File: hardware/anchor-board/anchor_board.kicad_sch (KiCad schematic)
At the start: 6 parts, among them U1 DWM3001C

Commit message: hw(anchor-board): capture §4.5 TLV75530 LDO; record MCU decision
- §4.5: U6 TLV75530 + C12/C13 1uF, C14 10uF, FB1 ferrite. The LDO OUT
  now drives the 3V0 rail, so the §4.1 3V0 PWR_FLAG placeholder is gone.
- New TLV75530 symbol (DQN / X2SON-4 pinout per the TLV755P datasheet).
- docs/mcu-tradeoff.md: decision to stay on the DWM3001C (not switch to
  DWM3000 + ESP32-C6), and solve developer onboarding by distributing
  pre-bootloadered boards. Includes the ESP32-C6 power model
  (~130-210 days vs ~290) and the antenna-delay self-cal finding.
- docs/datasheets/: 6 power-path datasheets committed (BQ24074, TPD4S014,
  TLV755P, DW01A, FS8205A, USB4105-GF-A).
- .kicad_pro filled out by KiCad on first open; .gitignore now excludes
  KiCad lock files and the VS Code .history/ dir.

ERC: 31 violations - 29 are U1's not-yet-captured §4.2-4.9 castellation
pins (expected WIP), 2 are footprint-not-found for the custom
DWM3001C / TLV75530 footprints (a layout-time task).
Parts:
- added C12, C13: 1uF, Capacitor_SMD:C_0603_1608Metric, symbol Device:C
- added C14: 10uF, Capacitor_SMD:C_0805_2012Metric, symbol Device:C
- added FB1: Ferrite Bead, Inductor_SMD:L_0603_1608Metric, symbol Device:L
- added U6: TLV75530, infinity-stumps:TLV75530_DQN, symbol infinity-stumps:TLV75530
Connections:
- net 3V0: now also C13.1, C14.1, U6.1 (OUT)
- net GND: now also C12.2, C13.2, C14.2, U6.2 (GND), U6.5 (PAD)
- new net VSYS: FB1.1
- new net VSYS_LDO: C12.1, FB1.2, U6.3 (EN), U6.4 (IN)

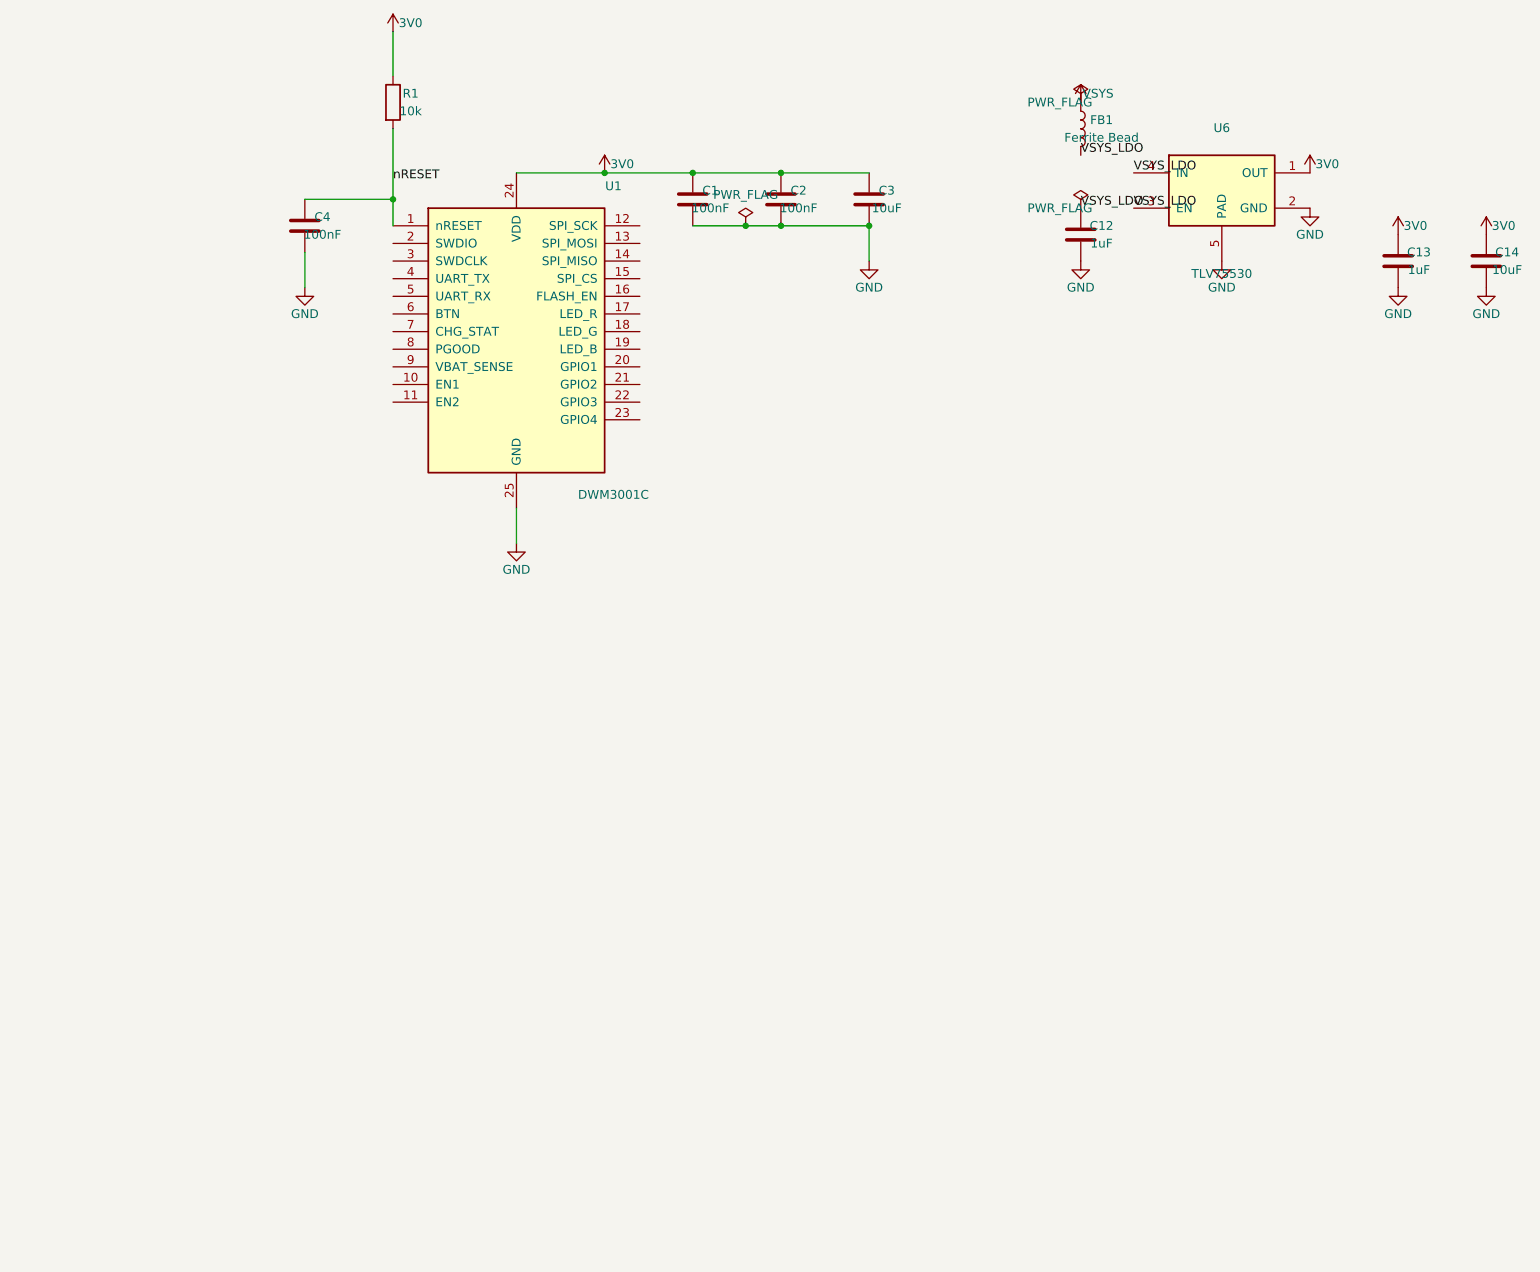
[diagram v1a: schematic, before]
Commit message: hw(anchor-board): capture §4.4 cell protection; add IC symbols; A3 sheet
- §4.4: BT1 18650 + U4 DW01A + U5 FS8205A + R13/C11/R14. DW01A+8205A
  back-to-back FET protection: cell+ -> VBAT, cell- -> BMINUS, the FET
  pair sits between BMINUS and system GND, DW_VCC fed via R13, current
  sense via R14, OD/OC gate drives, TD test pin no-connected.
- 5 new project symbols authored from docs/datasheets/: BQ24074, DW01A,
  FS8205A, USB4105-GF-A, TPD2E2U06. DW01A CS is a passive sense pin.
- Schematic sheet upgraded A4 -> A3 for the remaining functional blocks.

ERC: 32 violations - 29 are U1's not-yet-captured §4.2/4.3/4.6-4.8
castellation pins, 3 are footprint-not-found warnings for the custom
DWM3001C / TLV75530 / Keystone_1042 footprints (layout-time).
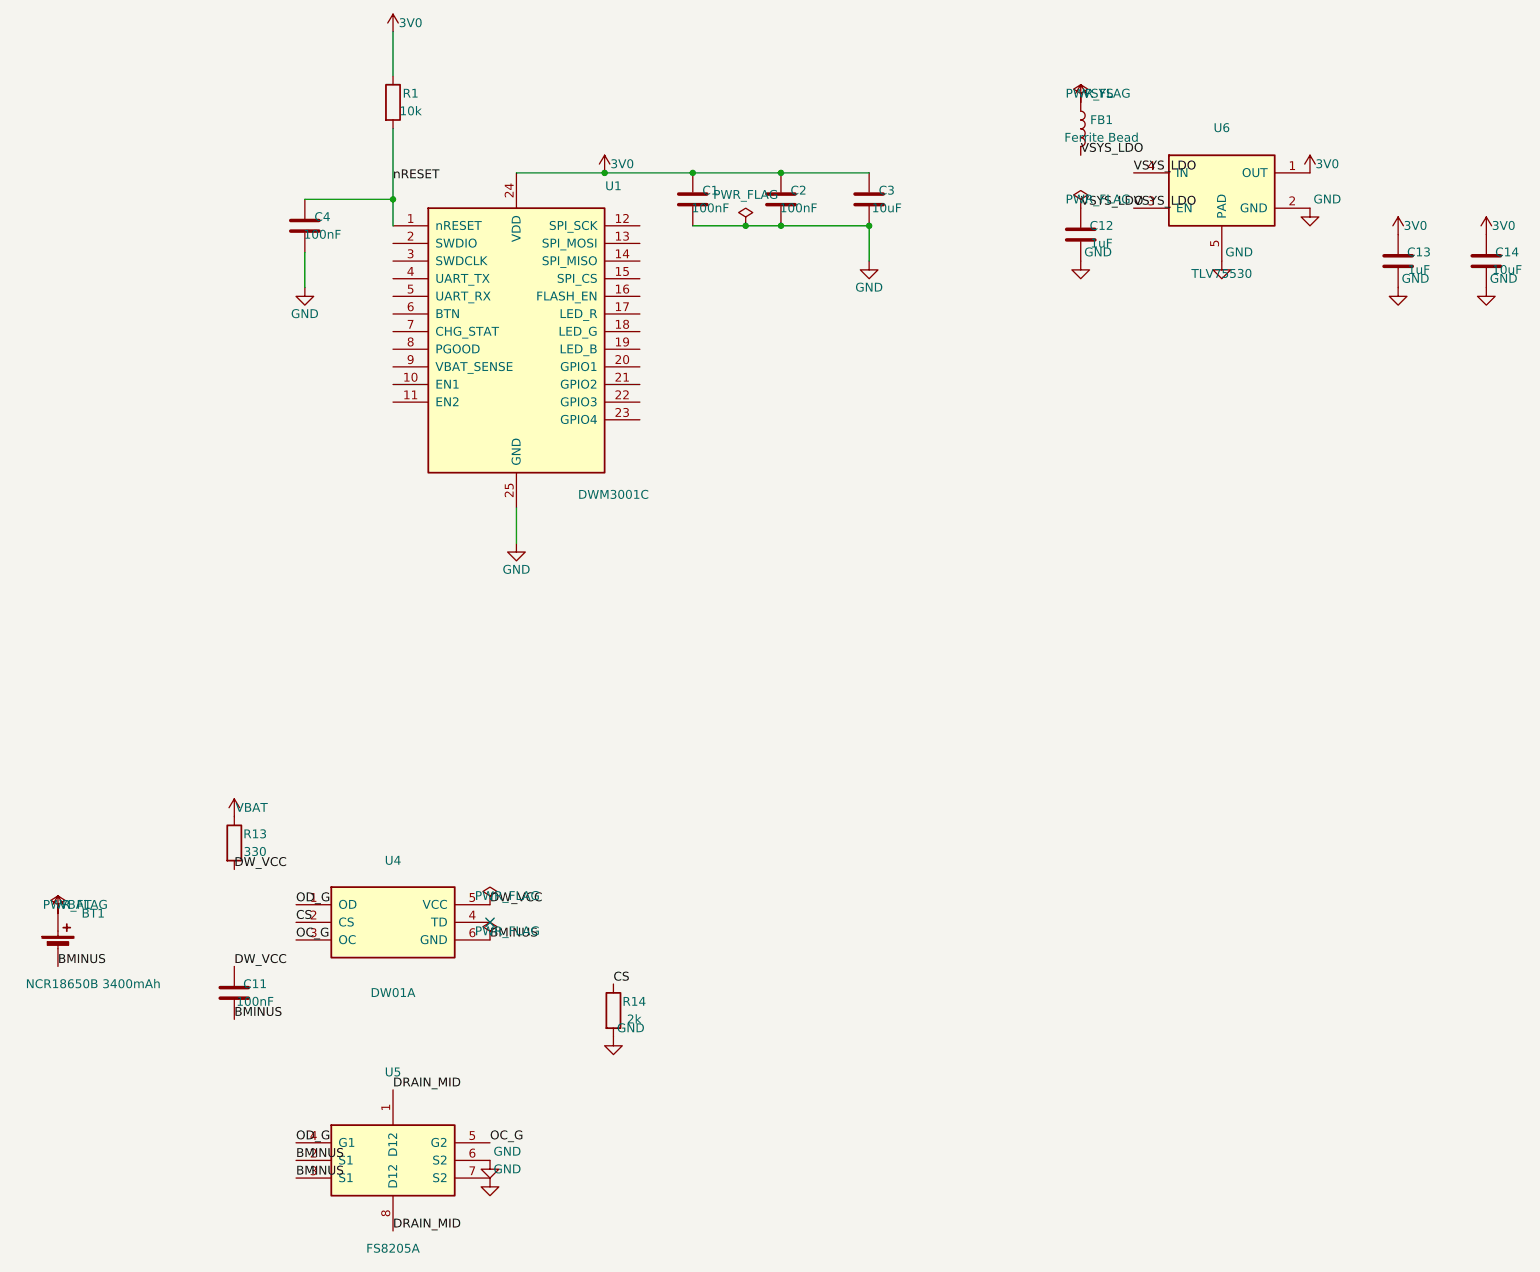
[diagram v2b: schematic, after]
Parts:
- added BT1: NCR18650B 3400mAh, infinity-stumps:Keystone_1042, symbol Device:Battery_Cell
- added C11: 100nF, Capacitor_SMD:C_0402_1005Metric, symbol Device:C
- added R13: 330, Resistor_SMD:R_0402_1005Metric, symbol Device:R
- added R14: 2k, Resistor_SMD:R_0402_1005Metric, symbol Device:R
- added U4: DW01A, Package_TO_SOT_SMD:SOT-23-6, symbol infinity-stumps:DW01A
- added U5: FS8205A, Package_SO:TSSOP-8_4.4x3mm_P0.65mm, symbol infinity-stumps:FS8205A
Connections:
- net GND: now also R14.2, U5.6 (S2), U5.7 (S2)
- new net BMINUS: BT1.2 (-), C11.2, U4.6 (GND), U5.2 (S1), U5.3 (S1)
- new net CS: R14.1, U4.2 (CS)
- new net DRAIN_MID: U5.1 (D12), U5.8 (D12)
- new net DW_VCC: C11.1, R13.2, U4.5 (VCC)
- new net OC_G: U4.3 (OC), U5.5 (G2)
- new net OD_G: U4.1 (OD), U5.4 (G1)
- new net VBAT: BT1.1 (+), R13.1
- no-connect marks 0 -> 1

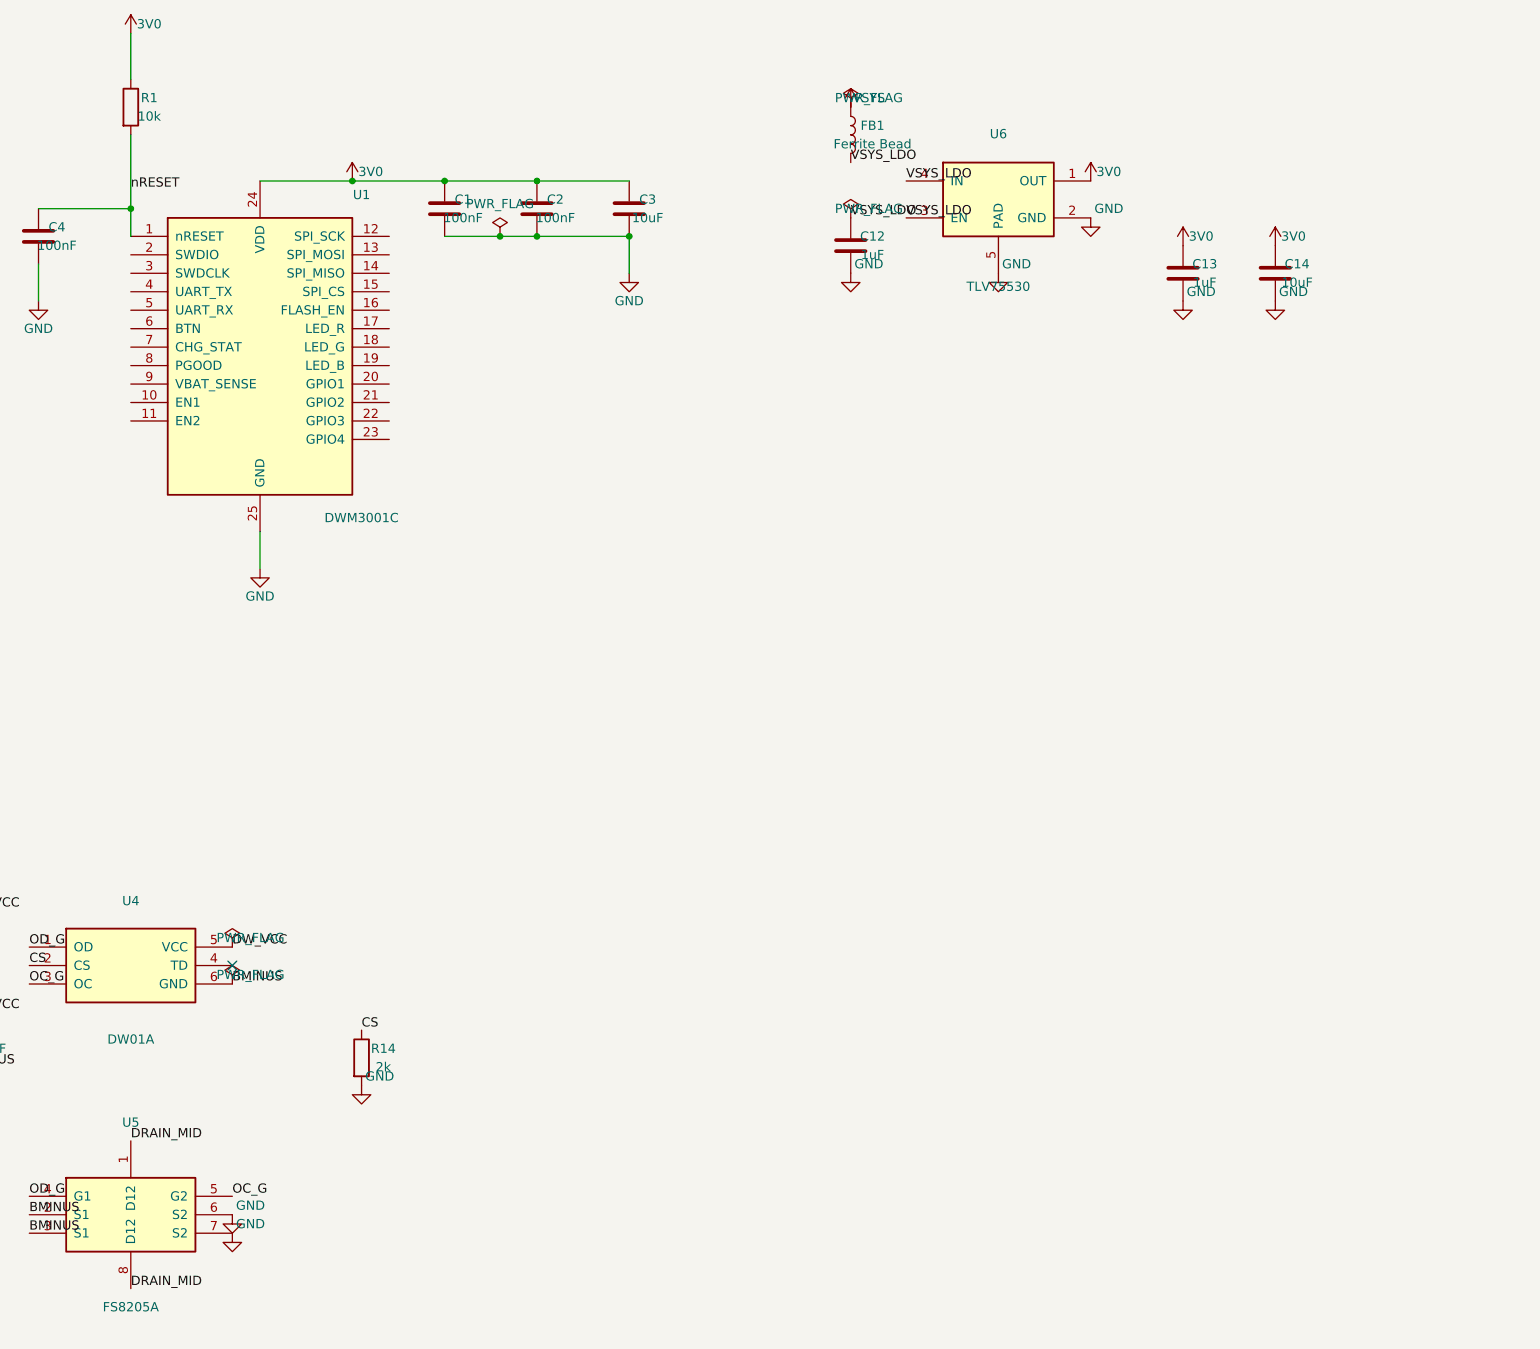
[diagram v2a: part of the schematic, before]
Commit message: hw(anchor-board): capture §4.3 BQ24074 charger
- §4.3: U3 BQ24074 + C8/C9/C10 IN/OUT/BAT caps, R5 909R ISET, R6 TMR,
  R7/R8 10k TS divider, R9/R10 10k CHG/PGOOD pull-ups, R11/R12 0R EN
  straps, plus R24/R25 for the ILIM/ITERM program pins (README §4.3 gaps).
- BQ24074 symbol: program / strap / sense pins set to passive; one of
  the dual OUT pins is passive so the shared node doesn't trip ERC.
- Power path: charger OUT now drives VSYS (replacing §4.5's placeholder
  flag); BAT -> VBAT; CHG/PGOOD reach U1, clearing 4 ERC errors.

ERC: 29 violations (was 32) - 25 are U1's not-yet-captured
§4.2/4.6/4.7/4.8 pins, 4 are footprint-not-found warnings.
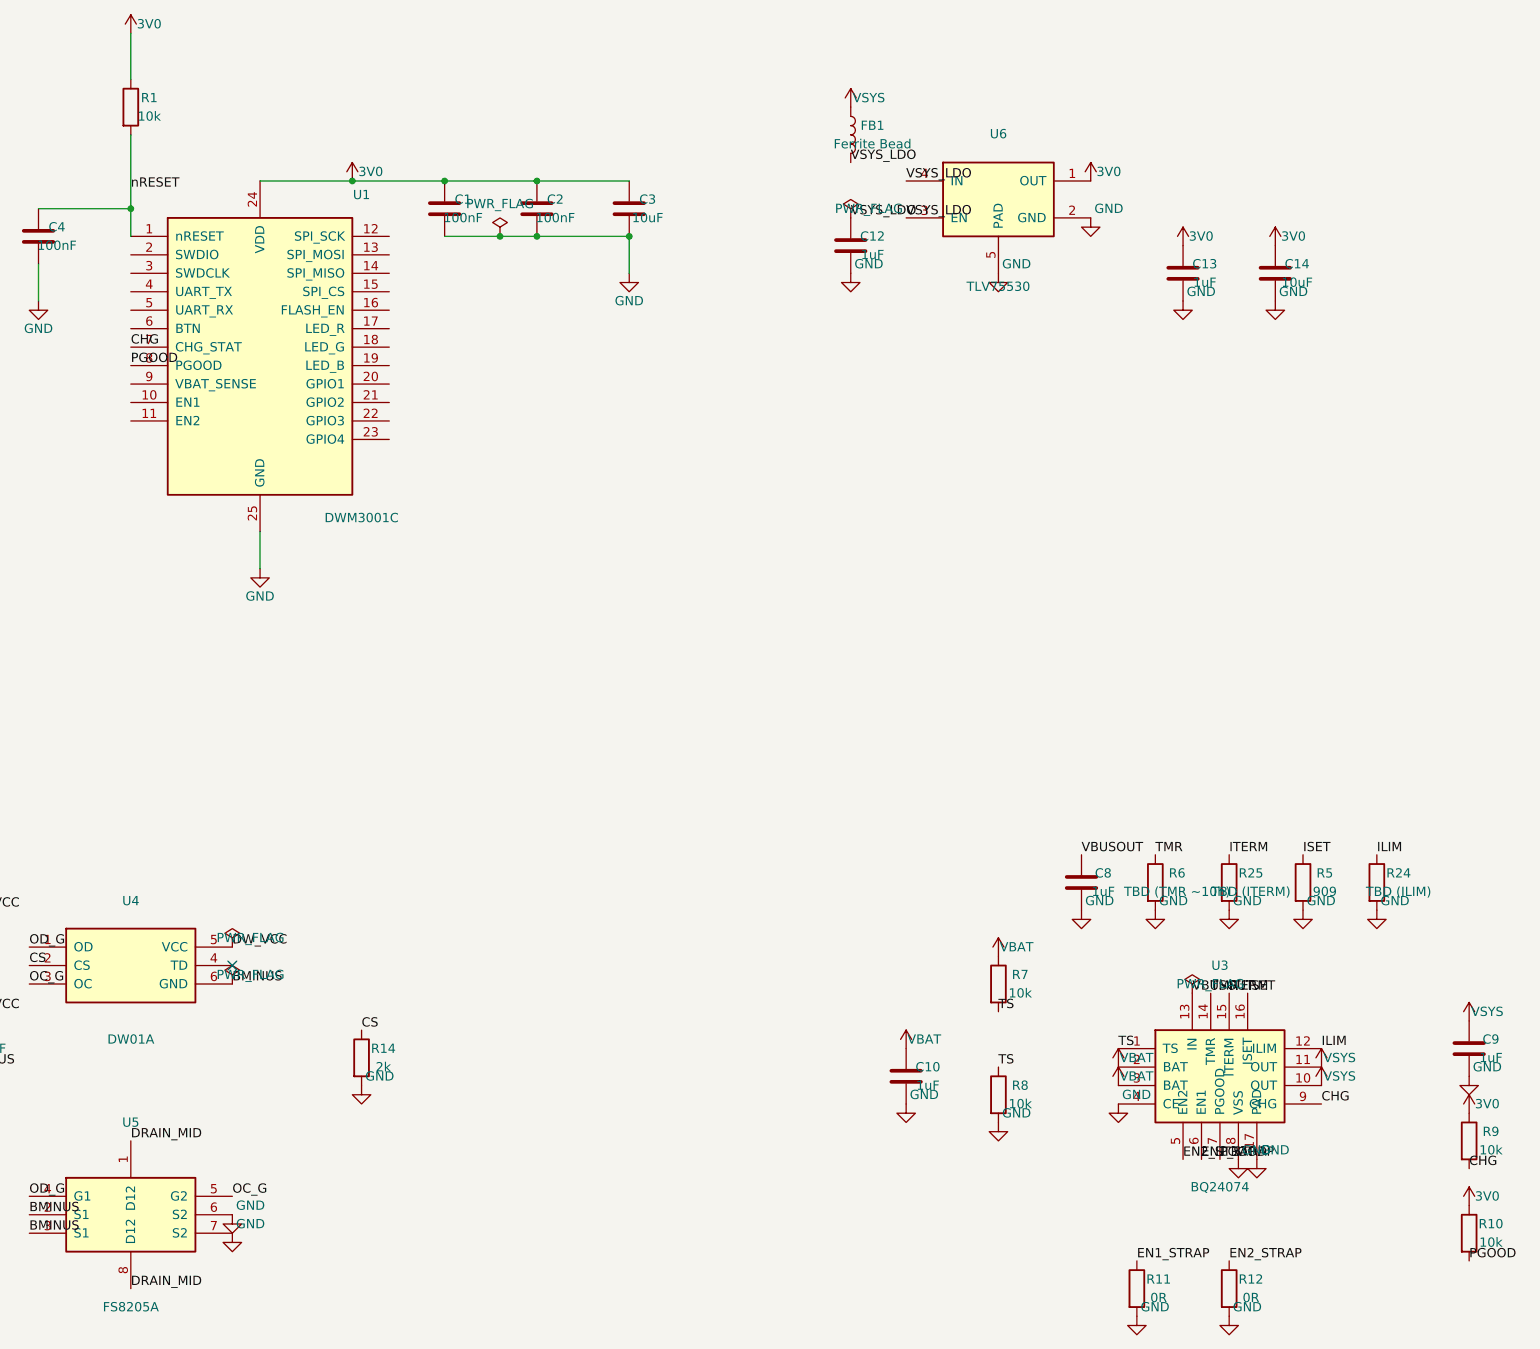
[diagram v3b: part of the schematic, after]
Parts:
- added C10, C8, C9: 1uF, Capacitor_SMD:C_0603_1608Metric, symbol Device:C
- added R10, R7, R8, R9: 10k, Resistor_SMD:R_0402_1005Metric, symbol Device:R
- added R11, R12: 0R, Resistor_SMD:R_0402_1005Metric, symbol Device:R
- added R24: TBD (ILIM), Resistor_SMD:R_0402_1005Metric, symbol Device:R
- added R25: TBD (ITERM), Resistor_SMD:R_0402_1005Metric, symbol Device:R
- added R5: 909, Resistor_SMD:R_0402_1005Metric, symbol Device:R
- added R6: TBD (TMR ~10h), Resistor_SMD:R_0402_1005Metric, symbol Device:R
- added U3: BQ24074, infinity-stumps:BQ24074_QFN16, symbol infinity-stumps:BQ24074
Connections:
- net 3V0: now also R10.1, R9.1
- net GND: now also C10.2, C8.2, C9.2, R11.2, R12.2, R24.2, R25.2, R5.2, R6.2, R8.2, U3.17 (PAD), U3.4 (CE), U3.8 (VSS)
- net VBAT: now also C10.1, R7.1, U3.2 (BAT), U3.3 (BAT)
- net VSYS: now also C9.1, U3.10 (OUT), U3.11 (OUT)
- net CHG: now reaches U1.7 (CHG_STAT)
- net CHG: now also R9.2, U3.9 (CHG)
- net PGOOD: now reaches U1.8 (PGOOD)
- net PGOOD: now also R10.2, U3.7 (PGOOD)
- new net EN1_STRAP: R11.1, U3.6 (EN1)
- new net EN2_STRAP: R12.1, U3.5 (EN2)
- new net ILIM: R24.1, U3.12 (ILIM)
- new net ISET: R5.1, U3.16 (ISET)
- new net ITERM: R25.1, U3.15 (ITERM)
- new net TMR: R6.1, U3.14 (TMR)
- new net TS: R7.2, R8.1, U3.1 (TS)
- new net VBUSOUT: C8.1, U3.13 (IN)
